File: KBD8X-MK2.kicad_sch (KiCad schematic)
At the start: 26 parts, among them J1 AVR-ISP-6, Q1 DSS60601MZ4-13, SW1 SW_Push, U1 ATmega32U4-MU, U2 PRTR5V0U2X, Y1 16MHz

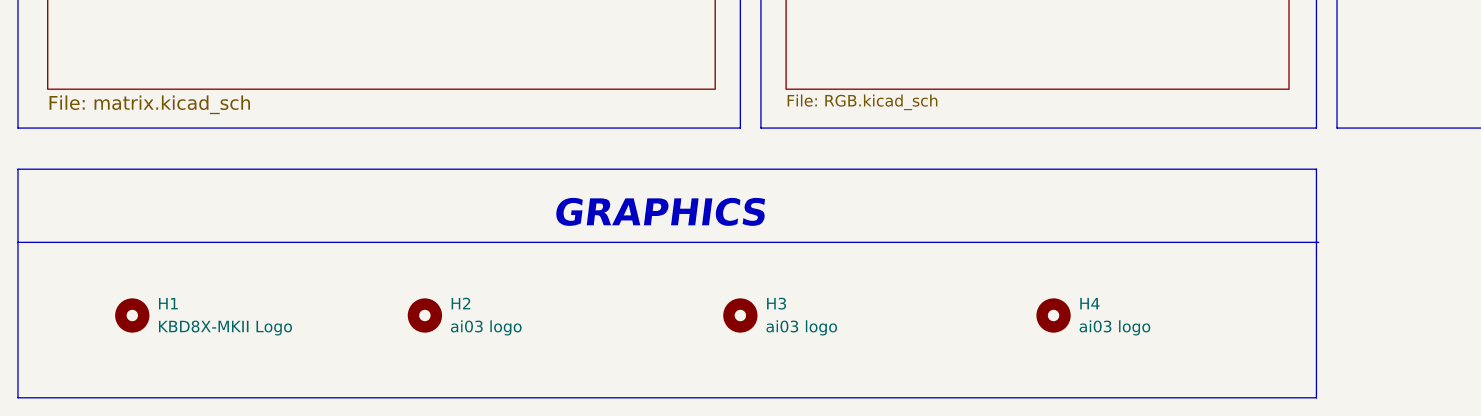
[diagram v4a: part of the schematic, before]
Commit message: Removed the solder joints on the front layer for the switches
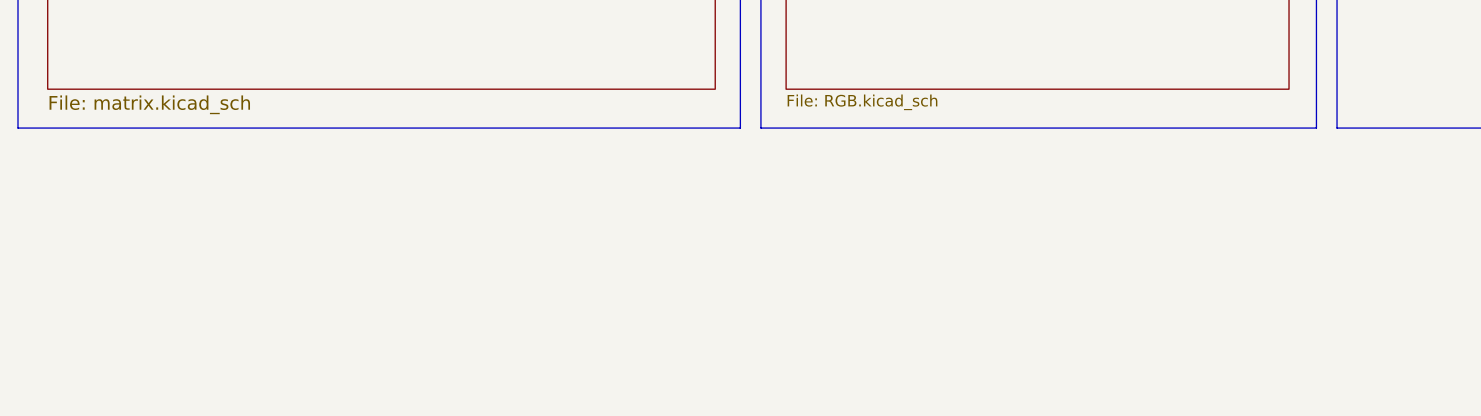
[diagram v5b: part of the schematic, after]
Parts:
- removed H1: KBD8X-MKII Logo, KBD8X_MK2_Graphics:kbd8x-logo, symbol Mechanical:MountingHole
- removed H2: ai03 logo, KBD8X_MK2_Graphics:ai-ring-6mm-FancyAss, symbol Mechanical:MountingHole
- removed H3: ai03 logo, KBD8X_MK2_Graphics:ai-ring-6mm-FancyAss-Mask, symbol Mechanical:MountingHole
- removed H4: ai03 logo, KBD8X_MK2_Graphics:ai-ring-6mm, symbol Mechanical:MountingHole
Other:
- note removed: "GRAPHICS"
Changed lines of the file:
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@@
-    (stroke (width 0) (type default) (color 0 0 0 0))
-  )
-  (polyline (pts (xy 17.78 166.116) (xy 162.052 166.116))
     (stroke (width 0) (type default) (color 0 0 0 0))
   )
@@
     (stroke (width 0) (type default) (color 0 0 0 0))
   )
-  (polyline (pts (xy 17.78 174.244) (xy 162.306 174.244))
-    (stroke (width 0) (type default) (color 0 0 0 0))
-  )
   (wire (pts (xy 196.85 74.422) (xy 201.93 74.422))
     (stroke (width 0) (type default) (color 0 0 0 0))
@@
     (stroke (width 0) (type default) (color 0 0 0 0))
   )
-  (polyline (pts (xy 162.052 166.116) (xy 162.052 191.516))
-    (stroke (width 0) (type default) (color 0 0 0 0))
-  )
   (wire (pts (xy 217.17 44.704) (xy 217.17 46.482))
     (stroke (width 0) (type default) (color 0 0 0 0))
@@
     (stroke (width 0) (type default) (color 0 0 0 0))
   )
-  (polyline (pts (xy 17.78 166.116) (xy 17.78 191.516))
-    (stroke (width 0) (type default) (color 0 0 0 0))
-  )
   (polyline (pts (xy 17.78 105.918) (xy 98.044 105.918))
     (stroke (width 0) (type default) (color 0 0 0 0))
@@
   )
   (wire (pts (xy 74.422 39.116) (xy 76.9112 39.116))
-    (stroke (width 0) (type default) (color 0 0 0 0))
-  )
-  (polyline (pts (xy 162.052 191.516) (xy 17.78 191.516))
     (stroke (width 0) (type default) (color 0 0 0 0))
   )
@@
   )
   (text "USB CIRCUITRY" (at 39.37 24.892 0)
-    (effects (font (size 3 3) (thickness 1.4) bold italic) (justify left bottom))
-  )
-  (text "GRAPHICS" (at 77.216 172.974 0)
     (effects (font (size 3 3) (thickness 1.4) bold italic) (justify left bottom))
   )
@@
     (pin "2")
   )
-  (symbol (lib_id "Mechanical:MountingHole") (at 30.48 182.372 0) (unit 1)
-    (in_bom yes) (on_board yes) (fields_autoplaced)
-    (property "Reference" "H1" (id 0) (at 33.274 181.1019 0)
-      (effects (font (size 1.27 1.27)) (justify left))
-    )
-    (property "Value" "KBD8X-MKII Logo" (id 1) (at 33.274 183.6419 0)
-      (effects (font (size 1.27 1.27)) (justify left))
-    )
-    (property "Footprint" "KBD8X_MK2_Graphics:kbd8x-logo" (id 2) (at 30.48 182.372 0)
-      (effects (font (size 1.27 1.27)) hide)
-    )
-    (property "Datasheet" "~" (id 3) (at 30.48 182.372 0)
-      (effects (font (size 1.27 1.27)) hide)
-    )
-  )
   (symbol (lib_id "power:PWR_FLAG") (at 211.2772 137.922 180) (unit 1)
     (in_bom yes) (on_board yes)
@@
     (pin "1")
   )
-  (symbol (lib_id "Mechanical:MountingHole") (at 98.044 182.372 0) (unit 1)
-    (in_bom yes) (on_board yes) (fields_autoplaced)
-    (property "Reference" "H3" (id 0) (at 100.838 181.1019 0)
-      (effects (font (size 1.27 1.27)) (justify left))
-    )
-    (property "Value" "ai03 logo" (id 1) (at 100.838 183.6419 0)
-      (effects (font (size 1.27 1.27)) (justify left))
-    )
-    (property "Footprint" "KBD8X_MK2_Graphics:ai-ring-6mm-FancyAss-Mask" (id 2) (at 98.044 182.372 0)
-      (effects (font (size 1.27 1.27)) hide)
-    )
-    (property "Datasheet" "~" (id 3) (at 98.044 182.372 0)
-      (effects (font (size 1.27 1.27)) hide)
-    )
-  )
   (symbol (lib_id "power:PWR_FLAG") (at 76.9112 39.116 180) (unit 1)
     (in_bom yes) (on_board yes)
@@
     (pin "1")
   )
-  (symbol (lib_id "Mechanical:MountingHole") (at 62.992 182.372 0) (unit 1)
-    (in_bom yes) (on_board yes) (fields_autoplaced)
-    (property "Reference" "H2" (id 0) (at 65.786 181.1019 0)
-      (effects (font (size 1.27 1.27)) (justify left))
-    )
-    (property "Value" "ai03 logo" (id 1) (at 65.786 183.6419 0)
-      (effects (font (size 1.27 1.27)) (justify left))
-    )
-    (property "Footprint" "KBD8X_MK2_Graphics:ai-ring-6mm-FancyAss" (id 2) (at 62.992 182.372 0)
-      (effects (font (size 1.27 1.27)) hide)
-    )
-    (property "Datasheet" "~" (id 3) (at 62.992 182.372 0)
-      (effects (font (size 1.27 1.27)) hide)
-    )
-  )
   (symbol (lib_id "power:PWR_FLAG") (at 67.4116 39.116 180) (unit 1)
     (in_bom yes) (on_board yes)
@@
     )
     (pin "1")
-  )
-  (symbol (lib_id "Mechanical:MountingHole") (at 132.842 182.372 0) (unit 1)
-    (in_bom yes) (on_board yes) (fields_autoplaced)
-    (property "Reference" "H4" (id 0) (at 135.636 181.1019 0)
-      (effects (font (size 1.27 1.27)) (justify left))
-    )
-    (property "Value" "ai03 logo" (id 1) (at 135.636 183.6419 0)
-      (effects (font (size 1.27 1.27)) (justify left))
-    )
-    (property "Footprint" "KBD8X_MK2_Graphics:ai-ring-6mm" (id 2) (at 132.842 182.372 0)
-      (effects (font (size 1.27 1.27)) hide)
-    )
-    (property "Datasheet" "~" (id 3) (at 132.842 182.372 0)
-      (effects (font (size 1.27 1.27)) hide)
-    )
   )
   (sheet (at 21.082 109.22) (size 74.168 48.006) (fields_autoplaced)
@@
       (reference "F1") (unit 1) (value "500mA") (footprint "KBD8X_MK2_Components:Fuse_1206_3216Metric")
     )
-    (path "/71d17f52-5aa4-432c-a827-b75d27bb76a1"
-      (reference "H1") (unit 1) (value "KBD8X-MKII Logo") (footprint "KBD8X_MK2_Graphics:kbd8x-logo")
-    )
-    (path "/a7511c61-6aa3-4b1e-8d80-2b8fa3f0a1c6"
-      (reference "H2") (unit 1) (value "ai03 logo") (footprint "KBD8X_MK2_Graphics:ai-ring-6mm-FancyAss")
-    )
-    (path "/7deb0899-cd4d-4db8-882c-e3207b4c8bf7"
-      (reference "H3") (unit 1) (value "ai03 logo") (footprint "KBD8X_MK2_Graphics:ai-ring-6mm-FancyAss-Mask")
-    )
-    (path "/fea93171-f380-4939-bf54-9bdd0c3928fb"
-      (reference "H4") (unit 1) (value "ai03 logo") (footprint "KBD8X_MK2_Graphics:ai-ring-6mm")
-    )
     (path "/00000000-0000-0000-0000-00005b68d1be"
